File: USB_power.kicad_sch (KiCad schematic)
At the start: 28 parts, among them J15 USB_C_Receptacle_PowerOnly_6P, Q3 BSC084P03NS3GATMA1, Q4 BSC084P03NS3GATMA1, U4 CYPD3177-24LQ

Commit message: annotation and pcb outline
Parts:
- renumbered C38 to C56, C41 to C57, C39 to C58, C40 to C59, C42 to C60, C43 to C61, C44 to C62, C45 to C63, C46 to C64, D1 to D4, J15 to J14, Q3 to Q8, Q4 to Q9, R9 to R18, R10 to R19, R11 to R20, R3 to R21, R12 to R22, R13 to R23, R4 to R24, R14 to R25, R16 to R26, R18 to R27, R19 to R28, R15 to R29, R17 to R30, U4 to U3

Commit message: new caps and bit of layout
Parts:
- renumbered C56 to C57, C57 to C58, C58 to C59, C59 to C60, C60 to C61, C61 to C62, C62 to C63, C63 to C64, C64 to C65
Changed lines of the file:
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@@
 		(dnp no)
 		(fields_autoplaced yes)
-		(property "Reference" "C64"
+		(property "Reference" "C65"
 			(at 200.66 59.6901 0)
 			(effects
@@
 			(project "RSC_extension_board"
 				(path "/1f48ed4c-84ce-4e77-88fc-25bf92dcee2d/05204050-0c20-42af-9081-73af52e92f24"
-					(reference "C64")
+					(reference "C65")
 					(unit 1)
 				)
@@
 		(dnp no)
 		(fields_autoplaced yes)
-		(property "Reference" "C59"
+		(property "Reference" "C60"
 			(at 92.71 129.5401 0)
 			(effects
@@
 			(project "RSC_extension_board"
 				(path "/1f48ed4c-84ce-4e77-88fc-25bf92dcee2d/05204050-0c20-42af-9081-73af52e92f24"
-					(reference "C59")
+					(reference "C60")
 					(unit 1)
 				)
@@
 		(dnp no)
 		(fields_autoplaced yes)
-		(property "Reference" "C56"
+		(property "Reference" "C57"
 			(at 73.66 116.8401 0)
 			(effects
@@
 			(project "RSC_extension_board"
 				(path "/1f48ed4c-84ce-4e77-88fc-25bf92dcee2d/05204050-0c20-42af-9081-73af52e92f24"
-					(reference "C56")
+					(reference "C57")
 					(unit 1)
 				)
@@
 		(dnp no)
 		(fields_autoplaced yes)
-		(property "Reference" "C57"
+		(property "Reference" "C58"
 			(at 86.36 100.3301 0)
 			(effects
@@
 			(project "RSC_extension_board"
 				(path "/1f48ed4c-84ce-4e77-88fc-25bf92dcee2d/05204050-0c20-42af-9081-73af52e92f24"
-					(reference "C57")
+					(reference "C58")
 					(unit 1)
 				)
@@
 		(dnp no)
 		(fields_autoplaced yes)
-		(property "Reference" "C60"
+		(property "Reference" "C61"
 			(at 95.25 60.9601 0)
 			(effects
@@
 			(project "RSC_extension_board"
 				(path "/1f48ed4c-84ce-4e77-88fc-25bf92dcee2d/05204050-0c20-42af-9081-73af52e92f24"
-					(reference "C60")
+					(reference "C61")
 					(unit 1)
 				)
@@
 		(dnp no)
 		(fields_autoplaced yes)
-		(property "Reference" "C61"
+		(property "Reference" "C62"
 			(at 146.05 83.8201 0)
 			(effects
@@
 			(project "RSC_extension_board"
 				(path "/1f48ed4c-84ce-4e77-88fc-25bf92dcee2d/05204050-0c20-42af-9081-73af52e92f24"
-					(reference "C61")
+					(reference "C62")
 					(unit 1)
 				)
@@
 		(dnp no)
 		(fields_autoplaced yes)
-		(property "Reference" "C63"
+		(property "Reference" "C64"
 			(at 171.45 83.8201 0)
 			(effects
@@
 			(project "RSC_extension_board"
 				(path "/1f48ed4c-84ce-4e77-88fc-25bf92dcee2d/05204050-0c20-42af-9081-73af52e92f24"
-					(reference "C63")
+					(reference "C64")
 					(unit 1)
 				)
@@
 		(dnp no)
 		(fields_autoplaced yes)
-		(property "Reference" "C58"
+		(property "Reference" "C59"
 			(at 86.36 116.8401 0)
 			(effects
@@
 			(project "RSC_extension_board"
 				(path "/1f48ed4c-84ce-4e77-88fc-25bf92dcee2d/05204050-0c20-42af-9081-73af52e92f24"
-					(reference "C58")
+					(reference "C59")
 					(unit 1)
 				)
@@
 		(dnp no)
 		(fields_autoplaced yes)
-		(property "Reference" "C62"
+		(property "Reference" "C63"
 			(at 158.75 83.8201 0)
 			(effects
@@
 			(project "RSC_extension_board"
 				(path "/1f48ed4c-84ce-4e77-88fc-25bf92dcee2d/05204050-0c20-42af-9081-73af52e92f24"
-					(reference "C62")
+					(reference "C63")
 					(unit 1)
 				)

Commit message: 20v in
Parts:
- R19: value 5k1 -> 0
- R20: value 2k4 -> DNP; now not fitted
- R22: value DNP -> 0; now fitted
- R23: value 0 -> DNP; now not fitted
- R26: value 5k1 -> 2k4
- R29: value DNP -> 5k1; now fitted
- R30: value 0 -> 2k4
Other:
- note added: "20V 2.5A https://www.infineon.com/assets/row/public/documents/24/49/ infineon-ez-pd-bcr-datasheet-usb-type-c-port-controller-for-power-sinks-datasheet-en.pdf"
- note removed: "12V 3A https://www.infineon.com/assets/row/public/documents/24/49/ infineon-ez-pd-bcr-datasheet-usb-type-c-port-controller-for-power-sinks-datasheet-en.pdf"
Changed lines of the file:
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@@
 	(generator_version "9.0")
 	(paper "A4")
-	(text "12V 3A\nhttps://www.infineon.com/assets/row/public/documents/24/49/\ninfineon-ez-pd-bcr-datasheet-usb-type-c-port-controller-for-power-sinks-datasheet-en.pdf"
+	(text "20V 2.5A\nhttps://www.infineon.com/assets/row/public/documents/24/49/\ninfineon-ez-pd-bcr-datasheet-usb-type-c-port-controller-for-power-sinks-datasheet-en.pdf"
 		(exclude_from_sim no)
 		(at 168.656 141.732 0)
@@
 		(in_bom yes)
 		(on_board yes)
-		(dnp no)
+		(dnp yes)
 		(fields_autoplaced yes)
 		(property "Reference" "R23"
@@
 			)
 		)
-		(property "Value" "0"
+		(property "Value" "DNP"
 			(at 129.54 153.6699 0)
 			(effects
@@
 		(in_bom yes)
 		(on_board yes)
-		(dnp yes)
+		(dnp no)
 		(fields_autoplaced yes)
 		(property "Reference" "R22"
@@
 			)
 		)
-		(property "Value" "DNP"
+		(property "Value" "0"
 			(at 129.54 143.5099 0)
 			(effects
@@
 			)
 		)
-		(property "Value" "0"
+		(property "Value" "2k4"
 			(at 162.56 153.6699 0)
 			(effects
@@
 		(in_bom yes)
 		(on_board yes)
-		(dnp no)
+		(dnp yes)
 		(fields_autoplaced yes)
 		(property "Reference" "R20"
@@
 			)
 		)
-		(property "Value" "2k4"
+		(property "Value" "DNP"
 			(at 111.76 153.6699 0)
 			(effects
@@
 			)
 		)
-		(property "Value" "5k1"
+		(property "Value" "0"
 			(at 111.76 143.5099 0)
 			(effects
@@
 		(in_bom yes)
 		(on_board yes)
-		(dnp yes)
+		(dnp no)
 		(fields_autoplaced yes)
 		(property "Reference" "R29"
@@
 			)
 		)
-		(property "Value" "DNP"
+		(property "Value" "5k1"
 			(at 162.56 143.5099 0)
 			(effects
@@
 			)
 		)
-		(property "Value" "5k1"
+		(property "Value" "2k4"
 			(at 147.32 153.6699 0)
 			(effects

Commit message: 20v to 5v 4A times two
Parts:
- renumbered C57 to C47, C58 to C48, C59 to C49, C60 to C50, C61 to C51, C62 to C52, C63 to C53, C64 to C54, C65 to C55, D4 to D1, Q8 to Q3, Q9 to Q4, R19 to R10, R20 to R11, R21 to R12, R22 to R13, R23 to R14, R24 to R15, R25 to R16, R26 to R17, R27 to R18, R28 to R19, R29 to R20, R30 to R21, R18 to R9, U3 to U5
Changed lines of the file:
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@@
 		(dnp no)
 		(fields_autoplaced yes)
-		(property "Reference" "R27"
+		(property "Reference" "R18"
 			(at 151.13 113.0299 0)
 			(effects
@@
 			(project "RSC_extension_board"
 				(path "/1f48ed4c-84ce-4e77-88fc-25bf92dcee2d/05204050-0c20-42af-9081-73af52e92f24"
-					(reference "R27")
+					(reference "R18")
 					(unit 1)
 				)
@@
 		(dnp no)
 		(fields_autoplaced yes)
-		(property "Reference" "R28"
+		(property "Reference" "R19"
 			(at 160.02 96.52 90)
 			(effects
@@
 			(project "RSC_extension_board"
 				(path "/1f48ed4c-84ce-4e77-88fc-25bf92dcee2d/05204050-0c20-42af-9081-73af52e92f24"
-					(reference "R28")
+					(reference "R19")
 					(unit 1)
 				)
@@
 		(dnp no)
 		(fields_autoplaced yes)
-		(property "Reference" "C65"
+		(property "Reference" "C55"
 			(at 200.66 59.6901 0)
 			(effects
@@
 			(project "RSC_extension_board"
 				(path "/1f48ed4c-84ce-4e77-88fc-25bf92dcee2d/05204050-0c20-42af-9081-73af52e92f24"
-					(reference "C65")
+					(reference "C55")
 					(unit 1)
 				)
@@
 		(dnp no)
 		(fields_autoplaced yes)
-		(property "Reference" "C60"
+		(property "Reference" "C50"
 			(at 92.71 129.5401 0)
 			(effects
@@
 			(project "RSC_extension_board"
 				(path "/1f48ed4c-84ce-4e77-88fc-25bf92dcee2d/05204050-0c20-42af-9081-73af52e92f24"
-					(reference "C60")
+					(reference "C50")
 					(unit 1)
 				)
@@
 		(on_board yes)
 		(dnp no)
-		(property "Reference" "Q9"
+		(property "Reference" "Q4"
 			(at 173.228 39.37 0)
 			(effects
@@
 			(project "RSC_extension_board"
 				(path "/1f48ed4c-84ce-4e77-88fc-25bf92dcee2d/05204050-0c20-42af-9081-73af52e92f24"
-					(reference "Q9")
+					(reference "Q4")
 					(unit 1)
 				)
@@
 		(dnp yes)
 		(fields_autoplaced yes)
-		(property "Reference" "R23"
+		(property "Reference" "R14"
 			(at 129.54 151.1299 0)
 			(effects
@@
 			(project "RSC_extension_board"
 				(path "/1f48ed4c-84ce-4e77-88fc-25bf92dcee2d/05204050-0c20-42af-9081-73af52e92f24"
-					(reference "R23")
+					(reference "R14")
 					(unit 1)
 				)
@@
 		(dnp no)
 		(fields_autoplaced yes)
-		(property "Reference" "R22"
+		(property "Reference" "R13"
 			(at 129.54 140.9699 0)
 			(effects
@@
 			(project "RSC_extension_board"
 				(path "/1f48ed4c-84ce-4e77-88fc-25bf92dcee2d/05204050-0c20-42af-9081-73af52e92f24"
-					(reference "R22")
+					(reference "R13")
 					(unit 1)
 				)
@@
 		(dnp no)
 		(fields_autoplaced yes)
-		(property "Reference" "R25"
+		(property "Reference" "R16"
 			(at 147.32 140.9699 0)
 			(effects
@@
 			(project "RSC_extension_board"
 				(path "/1f48ed4c-84ce-4e77-88fc-25bf92dcee2d/05204050-0c20-42af-9081-73af52e92f24"
-					(reference "R25")
+					(reference "R16")
 					(unit 1)
 				)
@@
 		(dnp no)
 		(fields_autoplaced yes)
-		(property "Reference" "R18"
+		(property "Reference" "R9"
 			(at 106.68 58.4199 0)
 			(effects
@@
 			(project "RSC_extension_board"
 				(path "/1f48ed4c-84ce-4e77-88fc-25bf92dcee2d/05204050-0c20-42af-9081-73af52e92f24"
-					(reference "R18")
+					(reference "R9")
 					(unit 1)
 				)
@@
 		(dnp no)
 		(fields_autoplaced yes)
-		(property "Reference" "R24"
+		(property "Reference" "R15"
 			(at 138.43 57.1499 0)
 			(effects
@@
 			(project "RSC_extension_board"
 				(path "/1f48ed4c-84ce-4e77-88fc-25bf92dcee2d/05204050-0c20-42af-9081-73af52e92f24"
-					(reference "R24")
+					(reference "R15")
 					(unit 1)
 				)
@@
 		(dnp no)
 		(fields_autoplaced yes)
-		(property "Reference" "R30"
+		(property "Reference" "R21"
 			(at 162.56 151.1299 0)
 			(effects
@@
 			(project "RSC_extension_board"
 				(path "/1f48ed4c-84ce-4e77-88fc-25bf92dcee2d/05204050-0c20-42af-9081-73af52e92f24"
-					(reference "R30")
+					(reference "R21")
 					(unit 1)
 				)
@@
 		(dnp no)
 		(fields_autoplaced yes)
-		(property "Reference" "D4"
+		(property "Reference" "D1"
 			(at 151.13 57.1499 90)
 			(effects
@@
 			(project "RSC_extension_board"
 				(path "/1f48ed4c-84ce-4e77-88fc-25bf92dcee2d/05204050-0c20-42af-9081-73af52e92f24"
-					(reference "D4")
+					(reference "D1")
 					(unit 1)
 				)
@@
 		(dnp no)
 		(fields_autoplaced yes)
-		(property "Reference" "U3"
+		(property "Reference" "U5"
 			(at 126.6033 85.09 0)
 			(effects
@@
 			(project "RSC_extension_board"
 				(path "/1f48ed4c-84ce-4e77-88fc-25bf92dcee2d/05204050-0c20-42af-9081-73af52e92f24"
-					(reference "U3")
+					(reference "U5")
 					(unit 1)
 				)
@@
 		(dnp no)
 		(fields_autoplaced yes)
-		(property "Reference" "C57"
+		(property "Reference" "C47"
 			(at 73.66 116.8401 0)
 			(effects
@@
 			(project "RSC_extension_board"
 				(path "/1f48ed4c-84ce-4e77-88fc-25bf92dcee2d/05204050-0c20-42af-9081-73af52e92f24"
-					(reference "C57")
+					(reference "C47")
 					(unit 1)
 				)
@@
 		(dnp no)
 		(fields_autoplaced yes)
-		(property "Reference" "C58"
+		(property "Reference" "C48"
 			(at 86.36 100.3301 0)
 			(effects
@@
 			(project "RSC_extension_board"
 				(path "/1f48ed4c-84ce-4e77-88fc-25bf92dcee2d/05204050-0c20-42af-9081-73af52e92f24"
-					(reference "C58")
+					(reference "C48")
 					(unit 1)
 				)
@@
 		(dnp yes)
 		(fields_autoplaced yes)
-		(property "Reference" "R20"
+		(property "Reference" "R11"
 			(at 111.76 151.1299 0)
 			(effects
@@
 			(project "RSC_extension_board"
 				(path "/1f48ed4c-84ce-4e77-88fc-25bf92dcee2d/05204050-0c20-42af-9081-73af52e92f24"
-					(reference "R20")
+					(reference "R11")
 					(unit 1)
 				)
@@
 		(on_board yes)
 		(dnp no)
-		(property "Reference" "Q8"
+		(property "Reference" "Q3"
 			(at 122.682 39.37 0)
 			(effects
@@
 			(project "RSC_extension_board"
 				(path "/1f48ed4c-84ce-4e77-88fc-25bf92dcee2d/05204050-0c20-42af-9081-73af52e92f24"
-					(reference "Q8")
+					(reference "Q3")
 					(unit 1)
 				)
@@
 		(dnp no)
 		(fields_autoplaced yes)
-		(property "Reference" "R19"
+		(property "Reference" "R10"
 			(at 111.76 140.9699 0)
 			(effects
@@
 			(project "RSC_extension_board"
 				(path "/1f48ed4c-84ce-4e77-88fc-25bf92dcee2d/05204050-0c20-42af-9081-73af52e92f24"
-					(reference "R19")
+					(reference "R10")
 					(unit 1)
 				)
@@
 		(dnp no)
 		(fields_autoplaced yes)
-		(property "Reference" "R29"
+		(property "Reference" "R20"
 			(at 162.56 140.9699 0)
 			(effects
@@
 			(project "RSC_extension_board"
 				(path "/1f48ed4c-84ce-4e77-88fc-25bf92dcee2d/05204050-0c20-42af-9081-73af52e92f24"
-					(reference "R29")
+					(reference "R20")
 					(unit 1)
 				)
@@
 		(dnp no)
 		(fields_autoplaced yes)
-		(property "Reference" "R21"
+		(property "Reference" "R12"
 			(at 121.92 74.9299 0)
 			(effects
@@
 			(project "RSC_extension_board"
 				(path "/1f48ed4c-84ce-4e77-88fc-25bf92dcee2d/05204050-0c20-42af-9081-73af52e92f24"
-					(reference "R21")
+					(reference "R12")
 					(unit 1)
 				)
@@
 		(dnp no)
 		(fields_autoplaced yes)
-		(property "Reference" "C61"
+		(property "Reference" "C51"
 			(at 95.25 60.9601 0)
 			(effects
@@
 			(project "RSC_extension_board"
 				(path "/1f48ed4c-84ce-4e77-88fc-25bf92dcee2d/05204050-0c20-42af-9081-73af52e92f24"
-					(reference "C61")
+					(reference "C51")
 					(unit 1)
 				)
@@
 		(dnp no)
 		(fields_autoplaced yes)
-		(property "Reference" "C62"
+		(property "Reference" "C52"
 			(at 146.05 83.8201 0)
 			(effects
@@
 			(project "RSC_extension_board"
 				(path "/1f48ed4c-84ce-4e77-88fc-25bf92dcee2d/05204050-0c20-42af-9081-73af52e92f24"
-					(reference "C62")
+					(reference "C52")
 					(unit 1)
 				)
@@
 		(dnp no)
 		(fields_autoplaced yes)
-		(property "Reference" "C64"
+		(property "Reference" "C54"
 			(at 171.45 83.8201 0)
 			(effects
@@
 			(project "RSC_extension_board"
 				(path "/1f48ed4c-84ce-4e77-88fc-25bf92dcee2d/05204050-0c20-42af-9081-73af52e92f24"
-					(reference "C64")
+					(reference "C54")
 					(unit 1)
 				)
@@
 		(dnp no)
 		(fields_autoplaced yes)
-		(property "Reference" "C59"
+		(property "Reference" "C49"
 			(at 86.36 116.8401 0)
 			(effects
@@
 			(project "RSC_extension_board"
 				(path "/1f48ed4c-84ce-4e77-88fc-25bf92dcee2d/05204050-0c20-42af-9081-73af52e92f24"
-					(reference "C59")
+					(reference "C49")
 					(unit 1)
 				)
@@
 		(dnp no)
 		(fields_autoplaced yes)
-		(property "Reference" "R26"
+		(property "Reference" "R17"
 			(at 147.32 151.1299 0)
 			(effects
@@
 			(project "RSC_extension_board"
 				(path "/1f48ed4c-84ce-4e77-88fc-25bf92dcee2d/05204050-0c20-42af-9081-73af52e92f24"
-					(reference "R26")
+					(reference "R17")
 					(unit 1)
 				)
@@
 		(dnp no)
 		(fields_autoplaced yes)
-		(property "Reference" "C63"
+		(property "Reference" "C53"
 			(at 158.75 83.8201 0)
 			(effects
@@
 			(project "RSC_extension_board"
 				(path "/1f48ed4c-84ce-4e77-88fc-25bf92dcee2d/05204050-0c20-42af-9081-73af52e92f24"
-					(reference "C63")
+					(reference "C53")
 					(unit 1)
 				)

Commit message: buck converter test pads and optional resistors
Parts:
- renumbered R9 to R17, R10 to R18, R11 to R19, R12 to R20, R13 to R21, R14 to R22, R15 to R23, R16 to R24, R17 to R25, R18 to R26, R19 to R27, R20 to R28, R21 to R29

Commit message: some footprint for LMR60440
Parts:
- renumbered R20 to R10, R21 to R11, R22 to R12, R23 to R13, R24 to R14, R25 to R15, R26 to R16, R27 to R17, R28 to R18, R29 to R19, R17 to R7, R18 to R8, R19 to R9

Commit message: pd controller
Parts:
- added J16: Conn_01x04, Connector_PinHeader_2.54mm:PinHeader_1x04_P2.54mm_Vertical, symbol Connector_Generic:Conn_01x04
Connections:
- net at U5.12 (HPI_SDA): now also J16.4 (Pin_4)
- net at U5.13 (HPI_SCL): now also J16.3 (Pin_3)
- net at U5.7 (~{HPI_INT}): now also J16.2 (Pin_2)
- net at U5.8 (GPIO_1): now also J16.1 (Pin_1)
- no-connect marks 5 -> 1
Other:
- moved on the sheet: R16
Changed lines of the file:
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@@
 		(at 121.92 87.63)
 	)
-	(no_connect
-		(at 139.7 110.49)
-	)
-	(no_connect
-		(at 139.7 107.95)
-	)
-	(no_connect
-		(at 139.7 115.57)
-	)
-	(no_connect
-		(at 139.7 113.03)
-	)
 	(wire
 		(pts
@@
 	(wire
 		(pts
-			(xy 139.7 118.11) (xy 148.59 118.11)
+			(xy 139.7 118.11) (xy 168.91 118.11)
 		)
 		(stroke
@@
 	(wire
 		(pts
+			(xy 144.78 107.95) (xy 139.7 107.95)
+		)
+		(stroke
+			(width 0)
+			(type default)
+		)
+	)
+	(wire
+		(pts
 			(xy 132.08 49.53) (xy 135.89 49.53)
 		)
@@
 	(wire
 		(pts
+			(xy 144.78 115.57) (xy 139.7 115.57)
+		)
+		(stroke
+			(width 0)
+			(type default)
+		)
+	)
+	(wire
+		(pts
 			(xy 104.14 49.53) (xy 106.68 49.53)
 		)
@@
 	(wire
 		(pts
+			(xy 144.78 113.03) (xy 139.7 113.03)
+		)
+		(stroke
+			(width 0)
+			(type default)
+		)
+	)
+	(wire
+		(pts
 			(xy 104.14 124.46) (xy 104.14 121.92)
 		)
@@
 	(wire
 		(pts
+			(xy 144.78 110.49) (xy 139.7 110.49)
+		)
+		(stroke
+			(width 0)
+			(type default)
+		)
+	)
+	(wire
+		(pts
 			(xy 104.14 63.5) (xy 104.14 68.58)
 		)
@@
 	(symbol
 		(lib_id "Device:R")
-		(at 148.59 114.3 180)
+		(at 168.91 114.3 180)
 		(unit 1)
 		(exclude_from_sim no)
@@
 		(fields_autoplaced yes)
 		(property "Reference" "R16"
-			(at 151.13 113.0299 0)
+			(at 171.45 113.0299 0)
 			(effects
 				(font
@@
 		)
 		(property "Value" "50k"
-			(at 151.13 115.5699 0)
+			(at 171.45 115.5699 0)
 			(effects
 				(font
@@
 		)
 		(property "Footprint" "Resistor_SMD:R_0603_1608Metric_Pad0.98x0.95mm_HandSolder"
-			(at 150.368 114.3 90)
+			(at 170.688 114.3 90)
 			(effects
 				(font
@@
 		)
 		(property "Datasheet" "~"
-			(at 148.59 114.3 0)
+			(at 168.91 114.3 0)
 			(effects
 				(font
@@
 		)
 		(property "Description" "Resistor"
-			(at 148.59 114.3 0)
+			(at 168.91 114.3 0)
 			(effects
 				(font
@@
 	(symbol
 		(lib_id "power:+3.3V")
-		(at 148.59 110.49 0)
+		(at 168.91 110.49 0)
 		(unit 1)
 		(exclude_from_sim no)
@@
 		(dnp no)
 		(property "Reference" "#PWR099"
-			(at 148.59 114.3 0)
+			(at 168.91 114.3 0)
 			(effects
 				(font
@@
 		)
 		(property "Value" "+3.3V"
-			(at 148.59 106.172 0)
+			(at 168.91 106.172 0)
 			(effects
 				(font
@@
 		)
 		(property "Footprint" ""
-			(at 148.59 110.49 0)
+			(at 168.91 110.49 0)
 			(effects
 				(font
@@
 		)
 		(property "Datasheet" ""
-			(at 148.59 110.49 0)
+			(at 168.91 110.49 0)
 			(effects
 				(font
@@
 		)
 		(property "Description" "Power symbol creates a global label with name \"+3.3V\""
-			(at 148.59 110.49 0)
+			(at 168.91 110.49 0)
 			(effects
 				(font
@@
 					(unit 1)
 				)
+			)
+		)
+	)
+	(symbol
+		(lib_id "Connector_Generic:Conn_01x04")
+		(at 149.86 110.49 0)
+		(unit 1)
+		(exclude_from_sim no)
+		(in_bom yes)
+		(on_board yes)
+		(dnp no)
+		(fields_autoplaced yes)
+		(property "Reference" "J16"
+			(at 152.4 110.4899 0)
+			(effects
+				(font
+					(size 1.27 1.27)
+				)
+				(justify left)
+			)
+		)
+		(property "Value" "Conn_01x04"
+			(at 152.4 113.0299 0)
+			(effects
+				(font
+					(size 1.27 1.27)
+				)
+				(justify left)
+			)
+		)
+		(property "Footprint" "Connector_PinHeader_2.54mm:PinHeader_1x04_P2.54mm_Vertical"
+			(at 149.86 110.49 0)
+			(effects
+				(font
+					(size 1.27 1.27)
+				)
+				(hide yes)
+			)
+		)
+		(property "Datasheet" "~"
+			(at 149.86 110.49 0)
+			(effects
+				(font
+					(size 1.27 1.27)
+				)
+				(hide yes)
+			)
+		)
+		(property "Description" "Generic connector, single row, 01x04, script generated (kicad-library-utils/schlib/autogen/connector/)"
+			(at 149.86 110.49 0)
+			(effects
+				(font
+					(size 1.27 1.27)
+				)
+				(hide yes)
+			)
+		)
+		(pin "3"
+		)
+		(pin "1"
+		)
+		(pin "2"
+		)
+		(pin "4"
+		)
+		(instances
+			(project "RSC_extension_board"
+				(path "/1f48ed4c-84ce-4e77-88fc-25bf92dcee2d/05204050-0c20-42af-9081-73af52e92f24"
+					(reference "J16")
+					(unit 1)
+				)

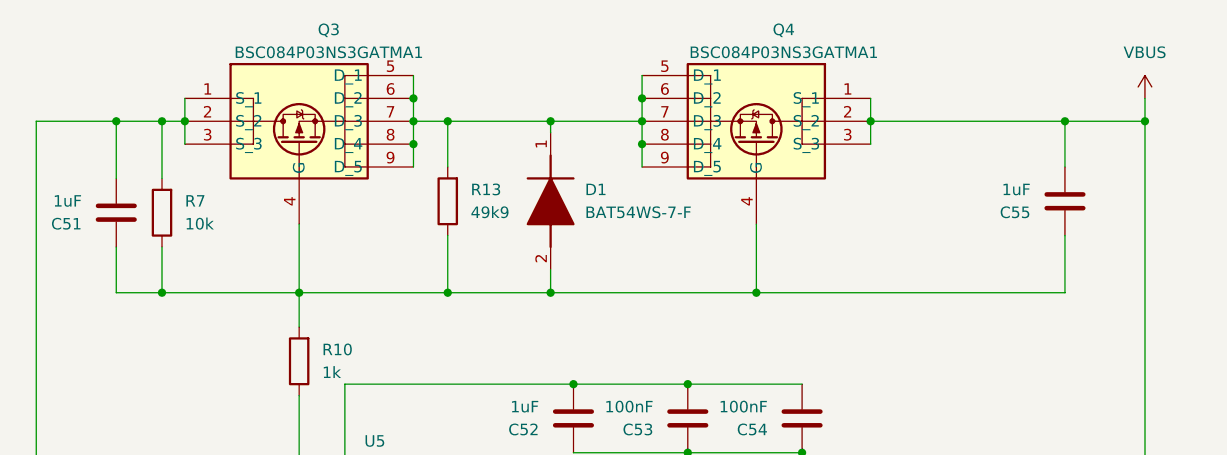
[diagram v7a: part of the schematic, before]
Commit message: DMP3013's for pd controller
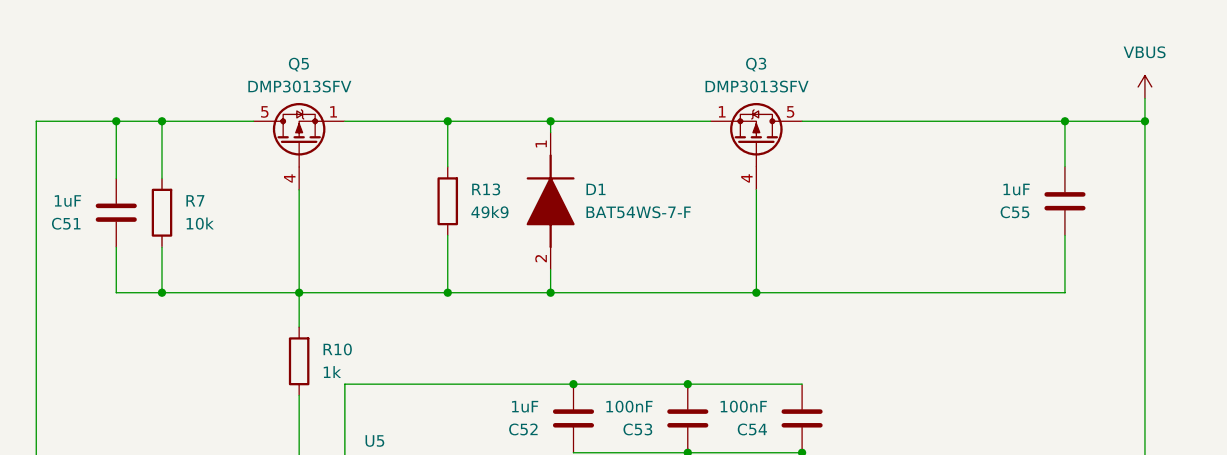
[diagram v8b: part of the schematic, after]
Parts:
- removed Q3, Q4: BSC084P03NS3GATMA1, BSC054N04NSG, symbol BSC084P03NS3GATMA1:BSC084P03NS3GATMA1
- added Q3, Q5: DMP3013SFV, Package_SON:Diodes_PowerDI3333-8, symbol Transistor_FET:DMP3013SFV
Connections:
- net VBUS: now also Q3.5 (D)
- net at C51.1, C55.1, D1.2 (A)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: now also Q3.4 (G), Q5.4 (G)
- net at C48.2, C51.2, J14.A9 (VBUS)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: now also Q5.5 (D)
- net at D1.1 (K), R13.2: now also Q3.1 (S), Q3.2 (S), Q3.3 (S), Q5.1 (S), Q5.2 (S), Q5.3 (S)
